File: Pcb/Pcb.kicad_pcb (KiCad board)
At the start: 2 copper layers, 152.3 x 104.7 mm, 120 parts, among them J1 ISP, J2 TRRS, Q1 2N7002, SW1 SW_Push, SW10 SW_Push, SW11 SW_Push, SW12 SW_Push, SW13 SW_Push, SW14 SW_Push, SW15 SW_Push, SW16 SW_Push, SW17 SW_Push, SW18 SW_Push, SW19 SW_Push, SW2 SW2, SW20 SW_Push, SW21 SW_Push, SW22 SW_Push, SW23 SW_Push, SW24 SW_Push, SW25 SW_Push, SW26 SW_Push, SW27 SW_Push, SW28 SW_Push, SW29 SW_Push, SW3 SW_Push, SW4 SW_Push, SW5 SW_Push, SW6 SW_Push, SW7 SW_Push, SW8 SW_Push, SW9 SW_Push, U1 ProMicro

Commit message: PCB update
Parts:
- added H4: MountHole, Used_Footprints:MountHole, F.Cu at (115.2, 100.3)
- added H5: MountHole, Used_Footprints:MountHole, F.Cu at (191.4, 112.2)
- added REFH1: MountHole, Used_Footprints:MountHole, F.Cu at (191.4, 55.0)
- added REFH2: MountHole, Used_Footprints:MountHole, F.Cu at (153.3, 51.5)
- added REFH3: MountHole, Used_Footprints:MountHole, F.Cu at (96.2, 82.5)
- moved Q1 214.6 mm to (212.4, 95.4), turned to 90 degrees
- moved SW29 188.9 mm to (220.9, 95.3)
- moved U1 164.0 mm to (220.6, 77.0)
- moved R30 133.3 mm to (220.9, 105.5), turned to 180 degrees
- moved R31 127.1 mm to (220.9, 100.0)
- moved J1 124.0 mm to (212.5, 99.5)
- moved R29 122.7 mm to (220.9, 102.8), turned to 180 degrees
- moved J2 0.77 mm to (221.3, 111.0)
- moved D10 0.30 mm to (154.9, 58.7)
- moved D12 0.30 mm to (193.0, 65.7)
- moved D16 0.30 mm to (154.9, 77.7)
- moved D18 0.30 mm to (193.0, 84.8)
- moved D22 0.30 mm to (154.9, 96.8)
- moved D24 0.30 mm to (193.0, 103.8)
- moved D27 0.30 mm to (193.0, 122.9)
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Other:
- outline, holes or cut-outs redrawn

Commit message: PCB route complete
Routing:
- net /LEDOut: track 0.00 -> 642.1 mm
- net VCC: track 0.00 -> 616.2 mm
- net /rowE: track 0.00 -> 268.8 mm, vias 0 -> 1
- net /col0: track 0.00 -> 236.3 mm, vias 0 -> 1
- net /col1: track 0.00 -> 202.5 mm
- net /rowA: track 0.00 -> 196.7 mm, vias 0 -> 1
- net /col4: track 0.00 -> 195.1 mm
- net /col3: track 0.00 -> 182.8 mm, vias 0 -> 1
- net /rowD: track 0.00 -> 179.2 mm
- net /rowB: track 0.00 -> 176.4 mm, vias 0 -> 1
- net /col2: track 0.00 -> 170.9 mm
- net /rowC: track 0.00 -> 168.2 mm
- net /col5: track 0.00 -> 162.2 mm
- net GND: track 0.00 -> 79.4 mm
- net RST: track 0.00 -> 63.4 mm
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
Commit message: Postrout optimization
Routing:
- added copper zone on B.Cu, net (none)
- added copper zone on F.Cu, net (none)
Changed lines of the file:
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@@
   (gr_line (start 134.26 112.02) (end 134.26 117.0685) (layer Edge.Cuts) (width 0.05))
   (gr_line (start 153.31 107.2575) (end 153.31 110.02) (layer Edge.Cuts) (width 0.05))
-  (gr_line (start 191.410001 35.87) (end 191.410001 36.156) (layer Edge.Cuts) (width 0.15))
+  (gr_line (start 191.410001 35.87) (end 191.410001 36.156) (layer Edge.Cuts) (width 0.05))
   (gr_line (start 211.51 134.8325) (end 228.51 134.8325) (layer Edge.Cuts) (width 0.05))
   (segment (start 98.5929 51.36) (end 98.5929 50.9029) (width 0.25) (layer F.Cu) (net 1))
@@
   (segment (start 214.4415 81.7071) (end 226.7949 81.7071) (width 0.25) (layer F.Cu) (net 82))
   (segment (start 226.7949 81.7071) (end 226.94 81.562) (width 0.25) (layer F.Cu) (net 82))
+  (zone (net 0) (net_name "") (layer F.Cu) (hatch edge 0.508)
+    (connect_pads (clearance 0.508))
+    (min_thickness 0.254)
+    (fill yes (arc_segments 32) (thermal_gap 0.508) (thermal_bridge_width 0.508))
+    (polygon
+      (pts
+        (xy 96.1 44.29) (xy 96.1 77.7) (xy 77.1 77.7) (xy 77.1 96.8) (xy 96.1 96.8)
+        (xy 96.1 120.6) (xy 115.31 120.6) (xy 115.31 118) (xy 134.3 118) (xy 134.3 111.1)
+        (xy 153.4 111.1) (xy 153.4 106.29) (xy 172.3 106.29) (xy 172.3 130.1) (xy 191.4 130.1)
+        (xy 191.4 132.4) (xy 210.4 132.4) (xy 210.4 134.9) (xy 229.6 134.9) (xy 229.6 58.6)
+        (xy 210.5 58.6) (xy 210.5 37.1) (xy 191.5 37.1) (xy 191.5 34.8) (xy 172.4 34.8)
+        (xy 172.4 30.08) (xy 153.3 30.08) (xy 153.3 34.8) (xy 134.27 34.8) (xy 134.27 41.8)
+        (xy 115.2 41.8) (xy 115.2 44.3)
+      )
+    )
+  )
+  (zone (net 0) (net_name "") (layer B.Cu) (hatch edge 0.508)
+    (connect_pads (clearance 0.508))
+    (min_thickness 0.254)
+    (fill yes (arc_segments 32) (thermal_gap 0.508) (thermal_bridge_width 0.508))
+    (polygon
+      (pts
+        (xy 96.1 44.29) (xy 96.1 77.7) (xy 77.1 77.7) (xy 77.1 96.8) (xy 96.1 96.8)
+        (xy 96.1 120.6) (xy 115.31 120.6) (xy 115.31 118) (xy 134.3 118) (xy 134.3 111.1)
+        (xy 153.4 111.1) (xy 153.4 106.29) (xy 172.3 106.29) (xy 172.3 130.1) (xy 191.4 130.1)
+        (xy 191.4 132.4) (xy 210.4 132.4) (xy 210.4 134.9) (xy 229.6 134.9) (xy 229.6 58.6)
+        (xy 210.5 58.6) (xy 210.5 37.1) (xy 191.5 37.1) (xy 191.5 34.8) (xy 172.4 34.8)
+        (xy 172.4 30.08) (xy 153.3 30.08) (xy 153.3 34.8) (xy 134.27 34.8) (xy 134.27 41.8)
+        (xy 115.2 41.8) (xy 115.2 44.3)
+      )
+    )
+  )
 )

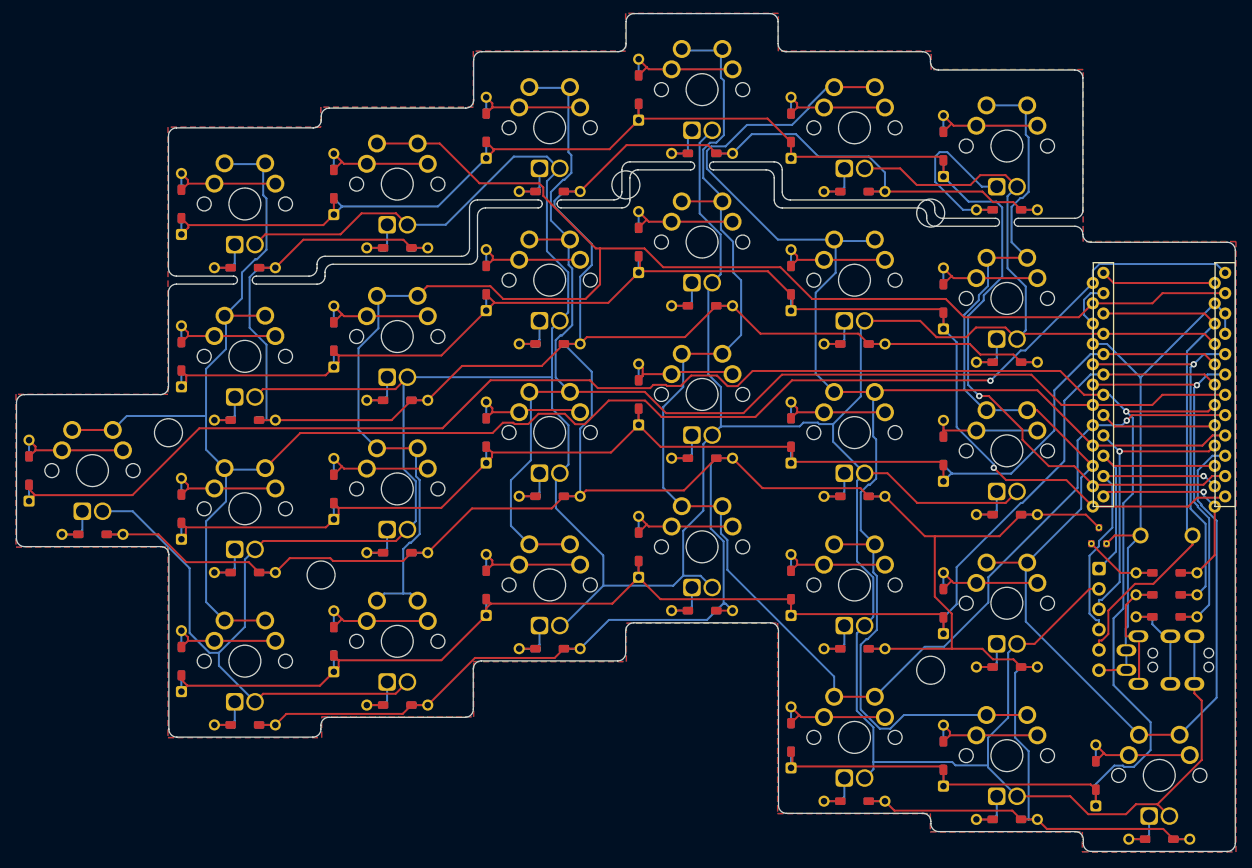
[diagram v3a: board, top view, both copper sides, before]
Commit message: Adapted for 3D print case.
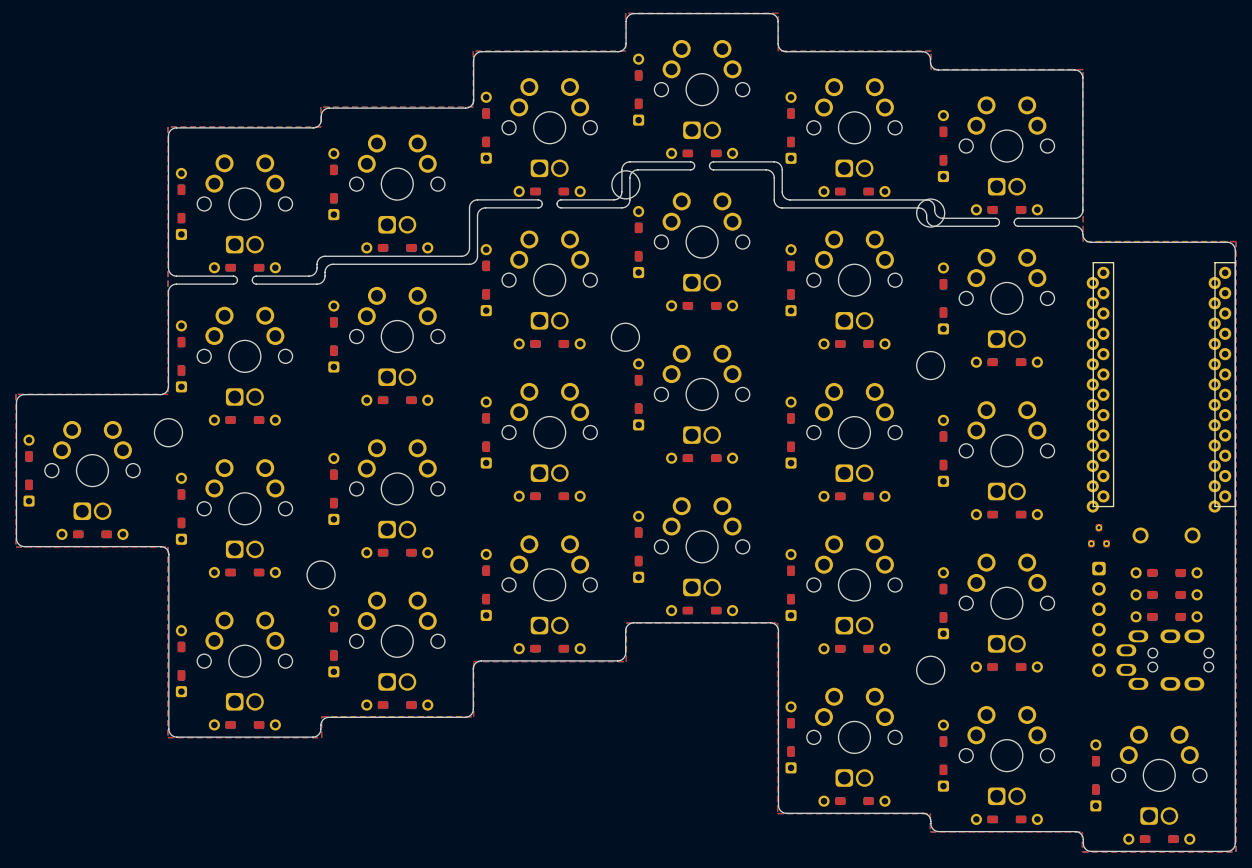
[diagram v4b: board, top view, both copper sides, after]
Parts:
- added REFH6: MountHole, Used_Footprints:MountHole, F.Cu at (191.4, 74.1)
- added REFH7: MountHole, Used_Footprints:MountHole, F.Cu at (153.3, 70.6)
- turned R30 to 0 degrees
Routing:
- net /LEDOut: track 642.1 -> 0.00 mm
- net VCC: track 616.2 -> 0.00 mm
- net /rowE: track 268.8 -> 0.00 mm, vias 1 -> 0
- net /col0: track 236.3 -> 0.00 mm, vias 1 -> 0
- net /col1: track 202.5 -> 0.00 mm
- net /rowA: track 196.7 -> 0.00 mm, vias 1 -> 0
- net /col4: track 195.1 -> 0.00 mm
- net /col3: track 182.8 -> 0.00 mm, vias 1 -> 0
- net /rowD: track 179.2 -> 0.00 mm
- net /rowB: track 176.4 -> 0.00 mm, vias 1 -> 0
- net /col2: track 170.9 -> 0.00 mm
- net /rowC: track 168.2 -> 0.00 mm
- net /col5: track 162.2 -> 0.00 mm
- net GND: track 79.4 -> 0.00 mm
- net RST: track 63.4 -> 0.00 mm
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
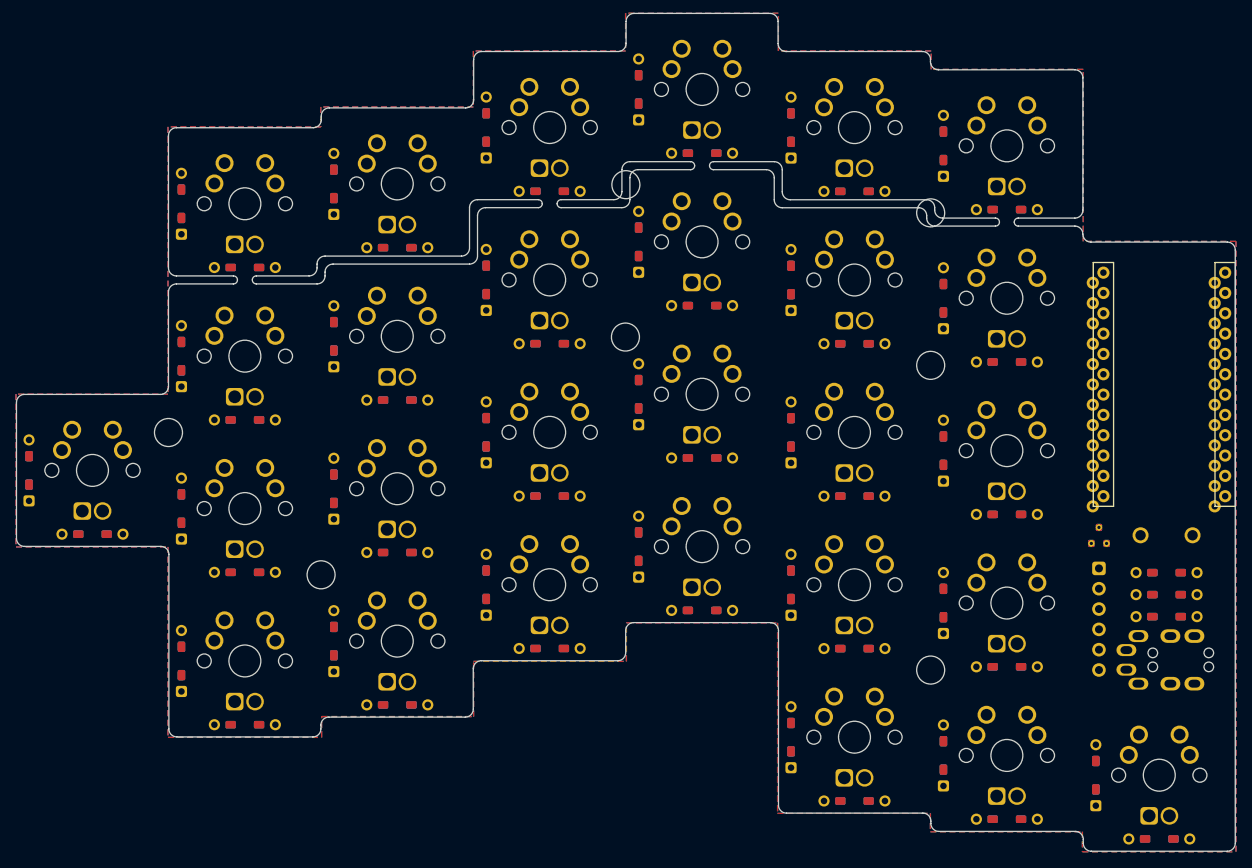
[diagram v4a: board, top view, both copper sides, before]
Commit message: Adapted for 3D case.
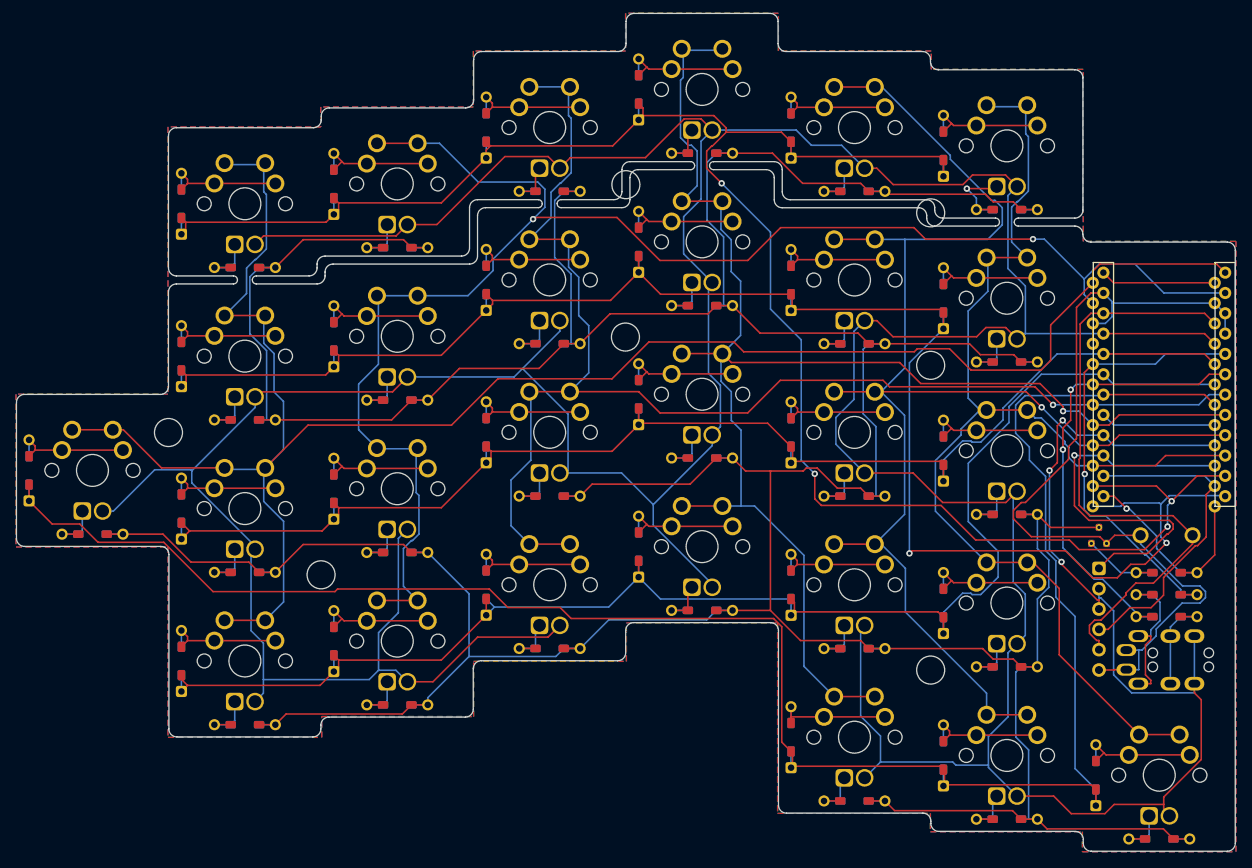
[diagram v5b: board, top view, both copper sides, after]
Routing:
- net /LEDOut: track 0.00 -> 632.6 mm
- net VCC: track 0.00 -> 621.0 mm
- net /rowE: track 0.00 -> 249.8 mm
- net /rowA: track 0.00 -> 247.7 mm, vias 0 -> 4
- net /col0: track 0.00 -> 242.5 mm
- net /rowB: track 0.00 -> 212.5 mm, vias 0 -> 2
- net /col1: track 0.00 -> 202.9 mm, vias 0 -> 2
- net /rowD: track 0.00 -> 187.5 mm
- net /col3: track 0.00 -> 187.1 mm, vias 0 -> 1
- net /col4: track 0.00 -> 184.0 mm, vias 0 -> 1
- net /col2: track 0.00 -> 170.4 mm, vias 0 -> 1
- net /rowC: track 0.00 -> 166.5 mm
- net /col5: track 0.00 -> 148.6 mm
- net GND: track 0.00 -> 110.6 mm
- net RST: track 0.00 -> 78.4 mm
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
